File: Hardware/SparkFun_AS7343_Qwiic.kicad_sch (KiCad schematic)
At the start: 39 parts, among them J1 Qwiic_RA, J2 Qwiic_RA, J3 Conn_01x06, Q1 BSS138, Q2 BSS138, U1 RT9080-1.8V, U2 AS7343

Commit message: remove extra directory - resave in kicad 9.0
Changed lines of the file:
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@@
 (kicad_sch
-	(version 20231120)
+	(version 20250114)
 	(generator "eeschema")
-	(generator_version "8.0")
+	(generator_version "9.0")
 	(paper "USLetter")
 	(title_block
@@
 		(comment 2 "Designed by: P. Lewis")
 	)
+	(text "Low Pass\n7.2KHz"
+		(exclude_from_sim no)
+		(at 59.69 41.91 0)
+		(effects
+			(font
+				(size 1.27 1.27)
+				(color 132 132 132 1)
+			)
+		)
+	)
+	(text "D3 is DNP\nUsers may populate\ntheir own PTH LED \nas desired."
+		(exclude_from_sim no)
+		(at 142.24 53.34 0)
+		(effects
+			(font
+				(size 1.27 1.27)
+				(color 132 132 132 1)
+			)
+		)
+	)
+	(text "1.8V Voltage Regulator"
+		(exclude_from_sim no)
+		(at 113.03 91.44 0)
+		(effects
+			(font
+				(size 3 3)
+			)
+		)
+	)
+	(text "I²C Logic Level Conversion"
+		(exclude_from_sim no)
+		(at 210.82 20.32 0)
+		(effects
+			(font
+				(size 3 3)
+			)
+		)
+	)
+	(text "Cut jumper to turn off power LED"
+		(exclude_from_sim no)
+		(at 24.638 135.128 0)
+		(effects
+			(font
+				(size 1.27 1.27)
+				(color 132 132 132 1)
+			)
+			(justify left bottom)
+		)
+	)
+	(text "Cut jumper to disable \non-board White LED."
+		(exclude_from_sim no)
+		(at 129.54 76.2 0)
+		(effects
+			(font
+				(size 1.27 1.27)
+				(color 132 132 132 1)
+			)
+		)
+	)
+	(text "Power LED"
+		(exclude_from_sim no)
+		(at 40.64 91.44 0)
+		(effects
+			(font
+				(size 3 3)
+			)
+		)
+	)
+	(text "Connectors"
+		(exclude_from_sim no)
+		(at 78.74 151.13 0)
+		(effects
+			(font
+				(size 3 3)
+			)
+		)
+	)
+	(text "Spectral Sensor AS7343"
+		(exclude_from_sim no)
+		(at 77.47 20.32 0)
+		(effects
+			(font
+				(size 3 3)
+			)
+		)
+	)
 	(junction
 		(at 71.12 60.96)
@@
 		)
 	)
-	(text "Low Pass\n7.2KHz"
-		(exclude_from_sim no)
-		(at 59.69 41.91 0)
-		(effects
-			(font
-				(size 1.27 1.27)
-				(color 132 132 132 1)
-			)
-		)
-	)
-	(text "D3 is DNP\nUsers may populate\ntheir own PTH LED \nas desired."
-		(exclude_from_sim no)
-		(at 142.24 53.34 0)
-		(effects
-			(font
-				(size 1.27 1.27)
-				(color 132 132 132 1)
-			)
-		)
-	)
-	(text "1.8V Voltage Regulator"
-		(exclude_from_sim no)
-		(at 113.03 91.44 0)
-		(effects
-			(font
-				(size 3 3)
-			)
-		)
-	)
-	(text "I²C Logic Level Conversion"
-		(exclude_from_sim no)
-		(at 210.82 20.32 0)
-		(effects
-			(font
-				(size 3 3)
-			)
-		)
-	)
-	(text "Cut jumper to turn off power LED"
-		(exclude_from_sim no)
-		(at 24.638 135.128 0)
-		(effects
-			(font
-				(size 1.27 1.27)
-				(color 132 132 132 1)
-			)
-			(justify left bottom)
-		)
-	)
-	(text "Cut jumper to disable \non-board White LED."
-		(exclude_from_sim no)
-		(at 129.54 76.2 0)
-		(effects
-			(font
-				(size 1.27 1.27)
-				(color 132 132 132 1)
-			)
-		)
-	)
-	(text "Power LED"
-		(exclude_from_sim no)
-		(at 40.64 91.44 0)
-		(effects
-			(font
-				(size 3 3)
-			)
-		)
-	)
-	(text "Connectors"
-		(exclude_from_sim no)
-		(at 78.74 151.13 0)
-		(effects
-			(font
-				(size 3 3)
-			)
-		)
-	)
-	(text "Spectral Sensor AS7343"
-		(exclude_from_sim no)
-		(at 77.47 20.32 0)
-		(effects
-			(font
-				(size 3 3)
-			)
-		)
-	)
 	(global_label "SDA"
 		(shape input)
@@
 		(on_board yes)
 		(dnp no)
-		(property "Reference" "#PWR0124"
+		(property "Reference" "#PWR0107"
 			(at 125.73 193.04 0)
 			(effects
@@
 		(on_board yes)
 		(dnp no)
-		(property "Reference" "#PWR0124"
+		(property "Reference" "#PWR0123"
 			(at 34.29 190.5 0)
 			(effects
@@
 		(on_board yes)
 		(dnp no)
-		(property "Reference" "#PWR0124"
+		(property "Reference" "#PWR0105"
 			(at 76.2 190.5 0)
 			(effects
@@
 		)
 	)
+	(embedded_fonts no)
 )

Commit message: PROD_IDs
-prod IDs for IC and white LED
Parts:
- U2: PROD_ID (none) -> IC-26195
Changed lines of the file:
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@@
 			)
 		)
-		(property "Datasheet" ""
+		(property "Datasheet" "https://look.ams-osram.com/m/5f2d27fff9a874d2/original/AS7343-14-Channel-Multi-Spectral-Sensor.pdf"
 			(at 80.518 70.866 0)
 			(effects
@@
 			)
 		)
-		(property "PROD_ID" ""
+		(property "PROD_ID" "IC-26195"
 			(at 81.534 77.47 0)
 			(effects

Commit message: I2C address in sch and bottom silk
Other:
- note added: "I2C ADDRESS: 0x39"
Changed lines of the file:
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@@
+		)
+	)
+	(text "I2C ADDRESS: 0x39"
+		(exclude_from_sim no)
+		(at 82.55 72.39 0)
+		(effects
+			(font
+				(size 1.27 1.27)
+				(color 132 132 132 1)
+			)
 		)
 	)

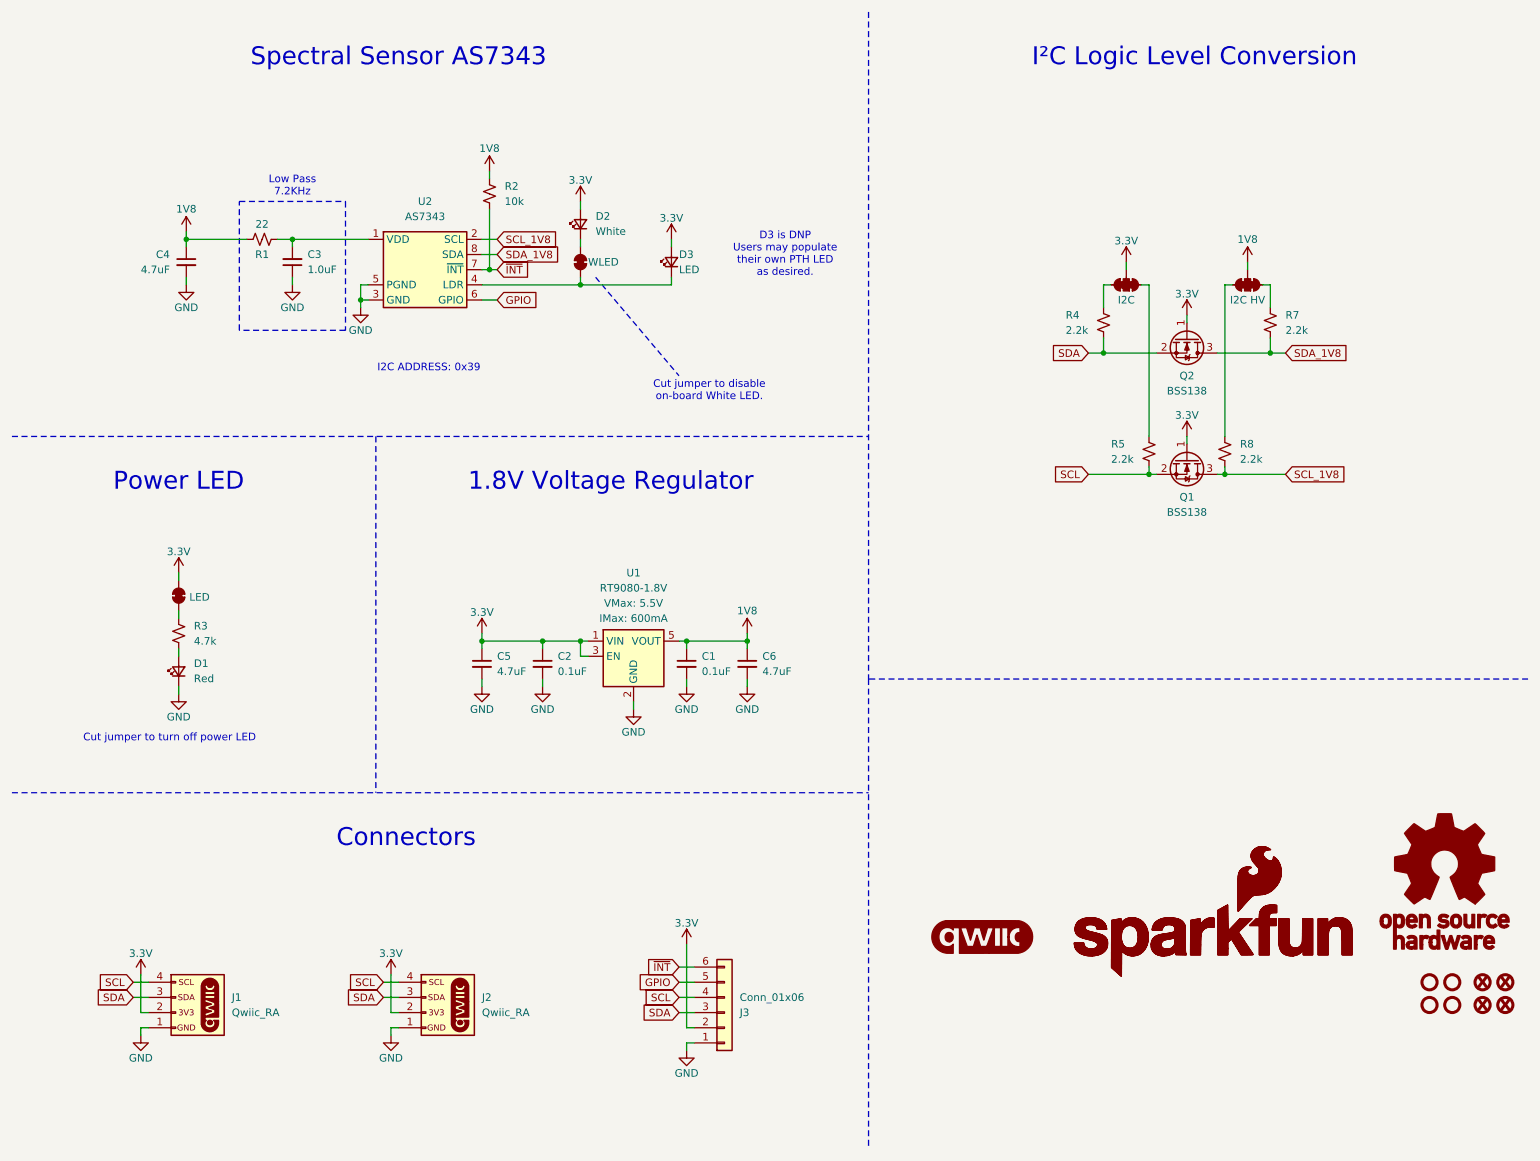
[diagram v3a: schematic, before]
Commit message: checklist run eng
-sch tightening
-vcc range added to sch
-removed PROD_ID from DNP LED
-add 1.8V testpoint
-increased copper to dimension clearance from 3 mils to 8 mils (avoiding sanding damage)
-nudged qwiic connectors inward from the edge by 5mils (avoiding sanding damage)
-updated pin one marker on IC from triangle to dot
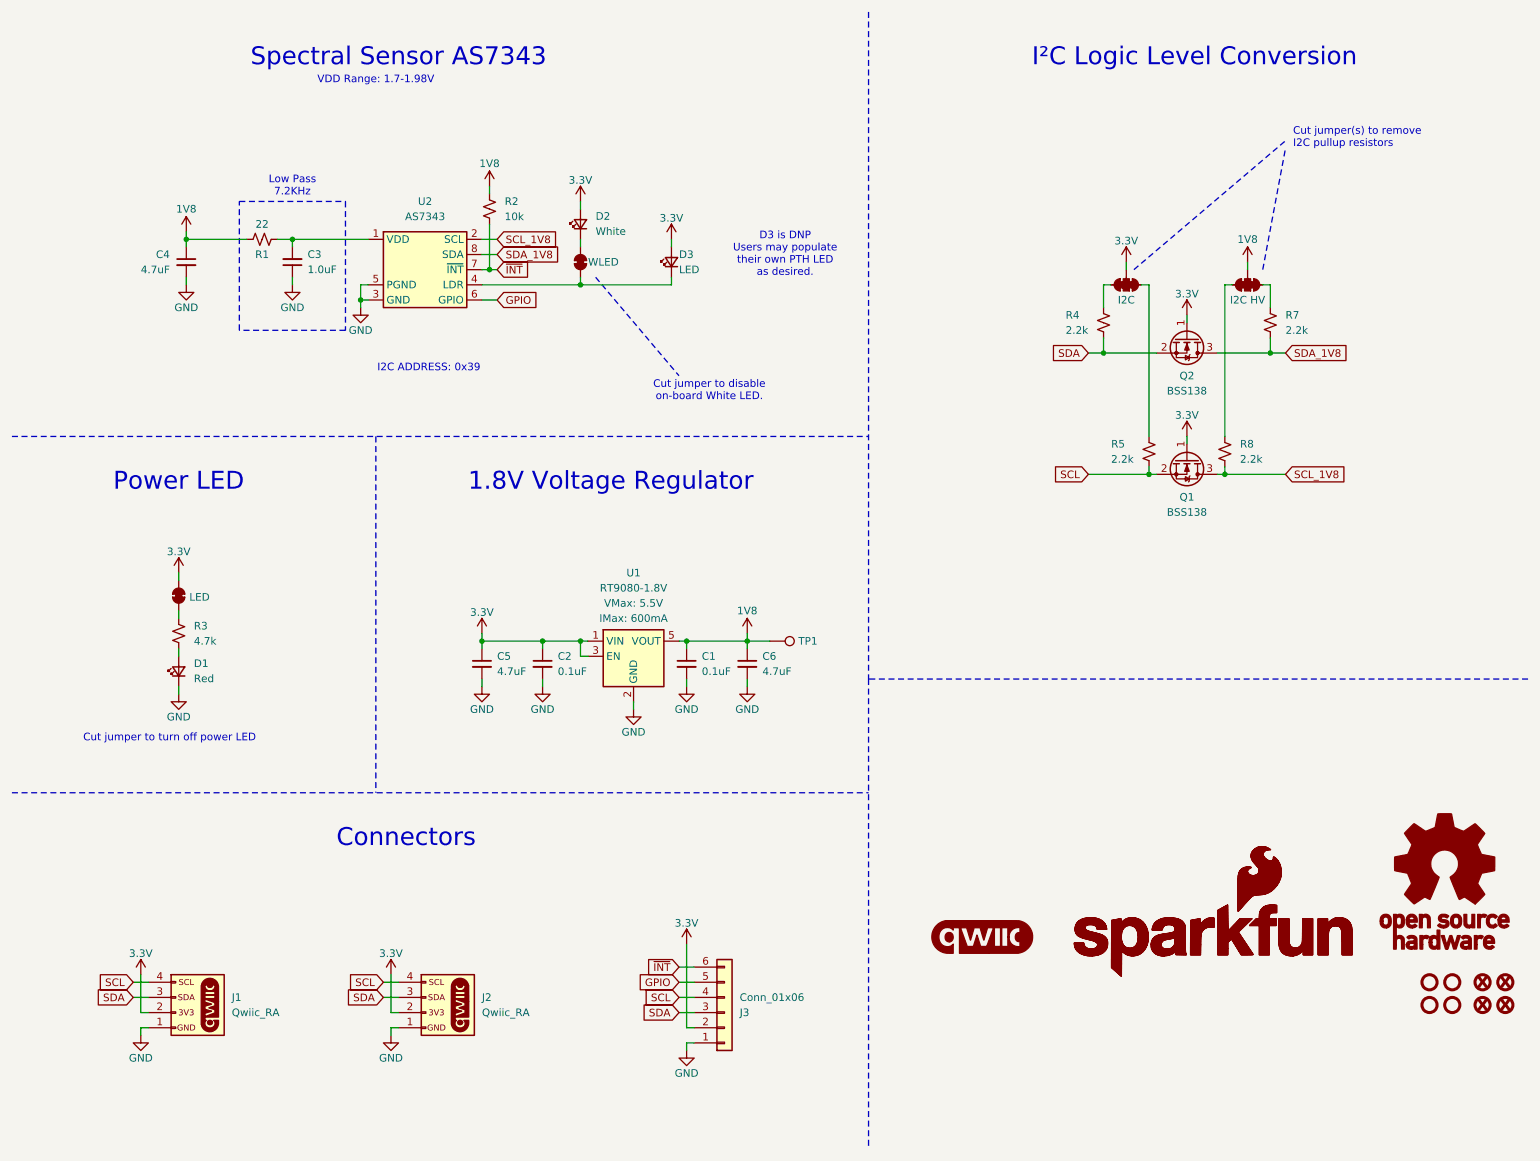
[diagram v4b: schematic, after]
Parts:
- added TP1: 1.0mm, SparkFun-Connector:TestPoint-1.0mm, symbol SparkFun-Connector:TestPoint_1.0mm
- D3: PROD_ID LED- -> (none)
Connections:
- net 1V8: now also TP1.1
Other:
- note added: "Cut jumper(s) to remove I2C pullup resistors"
- note added: "VDD Range: 1.7-1.98V"
- moved on the sheet: R2
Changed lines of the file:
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@@
 		)
 	)
+	(text "Cut jumper(s) to remove \nI2C pullup resistors"
+		(exclude_from_sim no)
+		(at 227.33 35.56 0)
+		(effects
+			(font
+				(size 1.27 1.27)
+				(color 132 132 132 1)
+			)
+			(justify left bottom)
+		)
+	)
 	(text "1.8V Voltage Regulator"
 		(exclude_from_sim no)
@@
 		)
 	)
+	(text "VDD Range: 1.7-1.98V"
+		(exclude_from_sim no)
+		(at 73.66 24.13 0)
+		(effects
+			(font
+				(size 1.27 1.27)
+				(color 132 132 132 1)
+			)
+		)
+	)
 	(text "Connectors"
 		(exclude_from_sim no)
@@
 	(wire
 		(pts
-			(xy 92.71 39.37) (xy 92.71 40.64)
+			(xy 92.71 41.91) (xy 92.71 43.18)
 		)
 		(stroke
@@
 	(wire
 		(pts
-			(xy 92.71 45.72) (xy 92.71 55.88)
+			(xy 92.71 48.26) (xy 92.71 55.88)
 		)
 		(stroke
@@
 		)
 	)
+	(polyline
+		(pts
+			(xy 200.66 55.88) (xy 226.06 34.29)
+		)
+		(stroke
+			(width 0)
+			(type dash)
+			(color 132 132 132 1)
+		)
+	)
 	(wire
 		(pts
@@
 	(wire
 		(pts
+			(xy 135.89 118.11) (xy 139.7 118.11)
+		)
+		(stroke
+			(width 0)
+			(type default)
+		)
+	)
+	(wire
+		(pts
 			(xy 91.44 118.11) (xy 101.6 118.11)
 		)
@@
 	(polyline
 		(pts
+			(xy 222.25 55.88) (xy 226.06 35.56)
+		)
+		(stroke
+			(width 0)
+			(type dash)
+			(color 132 132 132 1)
+		)
+	)
+	(polyline
+		(pts
 			(xy 50.8 66.04) (xy 50.8 44.45)
 		)
@@
 	)
 	(symbol
+		(lib_id "SparkFun-Connector:TestPoint_1.0mm")
+		(at 139.7 118.11 270)
+		(unit 1)
+		(exclude_from_sim no)
+		(in_bom yes)
+		(on_board yes)
+		(dnp no)
+		(property "Reference" "TP1"
+			(at 146.05 118.11 90)
+			(do_not_autoplace yes)
+			(effects
+				(font
+					(size 1.27 1.27)
+				)
+			)
+		)
+		(property "Value" "1.0mm"
+			(at 135.89 118.11 0)
+			(effects
+				(font
+					(size 1.27 1.27)
+				)
+				(hide yes)
+			)
+		)
+		(property "Footprint" "SparkFun-Connector:TestPoint-1.0mm"
+			(at 133.35 118.11 0)
+			(effects
+				(font
+					(size 1.27 1.27)
+				)
+				(hide yes)
+			)
+		)
+		(property "Datasheet" "~"
+			(at 132.08 118.11 0)
+			(effects
+				(font
+					(size 1.27 1.27)
+				)
+				(hide yes)
+			)
+		)
+		(property "Description" "Test Point"
+			(at 129.54 118.11 0)
+			(effects
+				(font
+					(size 1.27 1.27)
+				)
+				(hide yes)
+			)
+		)
+		(pin "1"
+		)
+		(instances
+			(project ""
+				(path "/e3dd3ae4-244d-4cba-9cca-5d2abf83f29a"
+					(reference "TP1")
+					(unit 1)
+				)
+			)
+		)
+	)
+	(symbol
 		(lib_id "SparkFun-Resistor:2.2k_0603")
 		(at 195.58 64.77 90)
@@
 	(symbol
 		(lib_id "SparkFun-Resistor:10k_0603")
-		(at 92.71 43.18 90)
+		(at 92.71 45.72 90)
 		(unit 1)
 		(exclude_from_sim no)
@@
 		(fields_autoplaced yes)
 		(property "Reference" "R2"
-			(at 95.25 41.9099 90)
+			(at 95.25 44.4499 90)
 			(effects
 				(font
@@
 		)
 		(property "Value" "10k"
-			(at 95.25 44.4499 90)
+			(at 95.25 46.9899 90)
 			(effects
 				(font
@@
 		)
 		(property "Footprint" "SparkFun-Resistor:R_0603_1608Metric"
-			(at 97.028 43.18 0)
+			(at 97.028 45.72 0)
 			(effects
 				(font
@@
 		)
 		(property "Datasheet" "https://www.vishay.com/docs/20035/dcrcwe3.pdf"
-			(at 101.6 43.18 0)
+			(at 101.6 45.72 0)
 			(effects
 				(font
@@
 		)
 		(property "Description" "Resistor"
-			(at 104.14 43.18 0)
+			(at 104.14 45.72 0)
 			(effects
 				(font
@@
 		)
 		(property "PROD_ID" "RES-00824"
-			(at 99.06 43.18 0)
+			(at 99.06 45.72 0)
 			(effects
 				(font
@@
 			)
 		)
-		(property "PROD_ID" "LED-"
-			(at 133.35 54.61 0)
-			(effects
-				(font
-					(size 1.27 1.27)
-				)
-				(hide yes)
-			)
-		)
 		(pin "2"
 		)
@@
 	(symbol
 		(lib_id "SparkFun-PowerSymbol:VCC")
-		(at 92.71 39.37 0)
+		(at 92.71 41.91 0)
 		(unit 1)
 		(exclude_from_sim no)
@@
 		(fields_autoplaced yes)
 		(property "Reference" "#PWR09"
-			(at 92.71 43.18 0)
+			(at 92.71 45.72 0)
 			(effects
 				(font
@@
 		)
 		(property "Value" "1V8"
-			(at 92.71 35.56 0)
+			(at 92.71 38.1 0)
 			(do_not_autoplace yes)
 			(effects
@@
 		)
 		(property "Footprint" ""
-			(at 92.71 39.37 0)
+			(at 92.71 41.91 0)
 			(effects
 				(font
@@
 		)
 		(property "Datasheet" ""
-			(at 92.71 39.37 0)
+			(at 92.71 41.91 0)
 			(effects
 				(font
@@
 		)
 		(property "Description" "Power symbol creates a global label with name \"VCC\""
-			(at 92.71 45.72 0)
+			(at 92.71 48.26 0)
 			(effects
 				(font

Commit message: more review catches
-Checked the properties box for DNP on D3, also exclude from BOM.
-sch cleanup
-removed isolation jumper for 1v8 i2c pullups
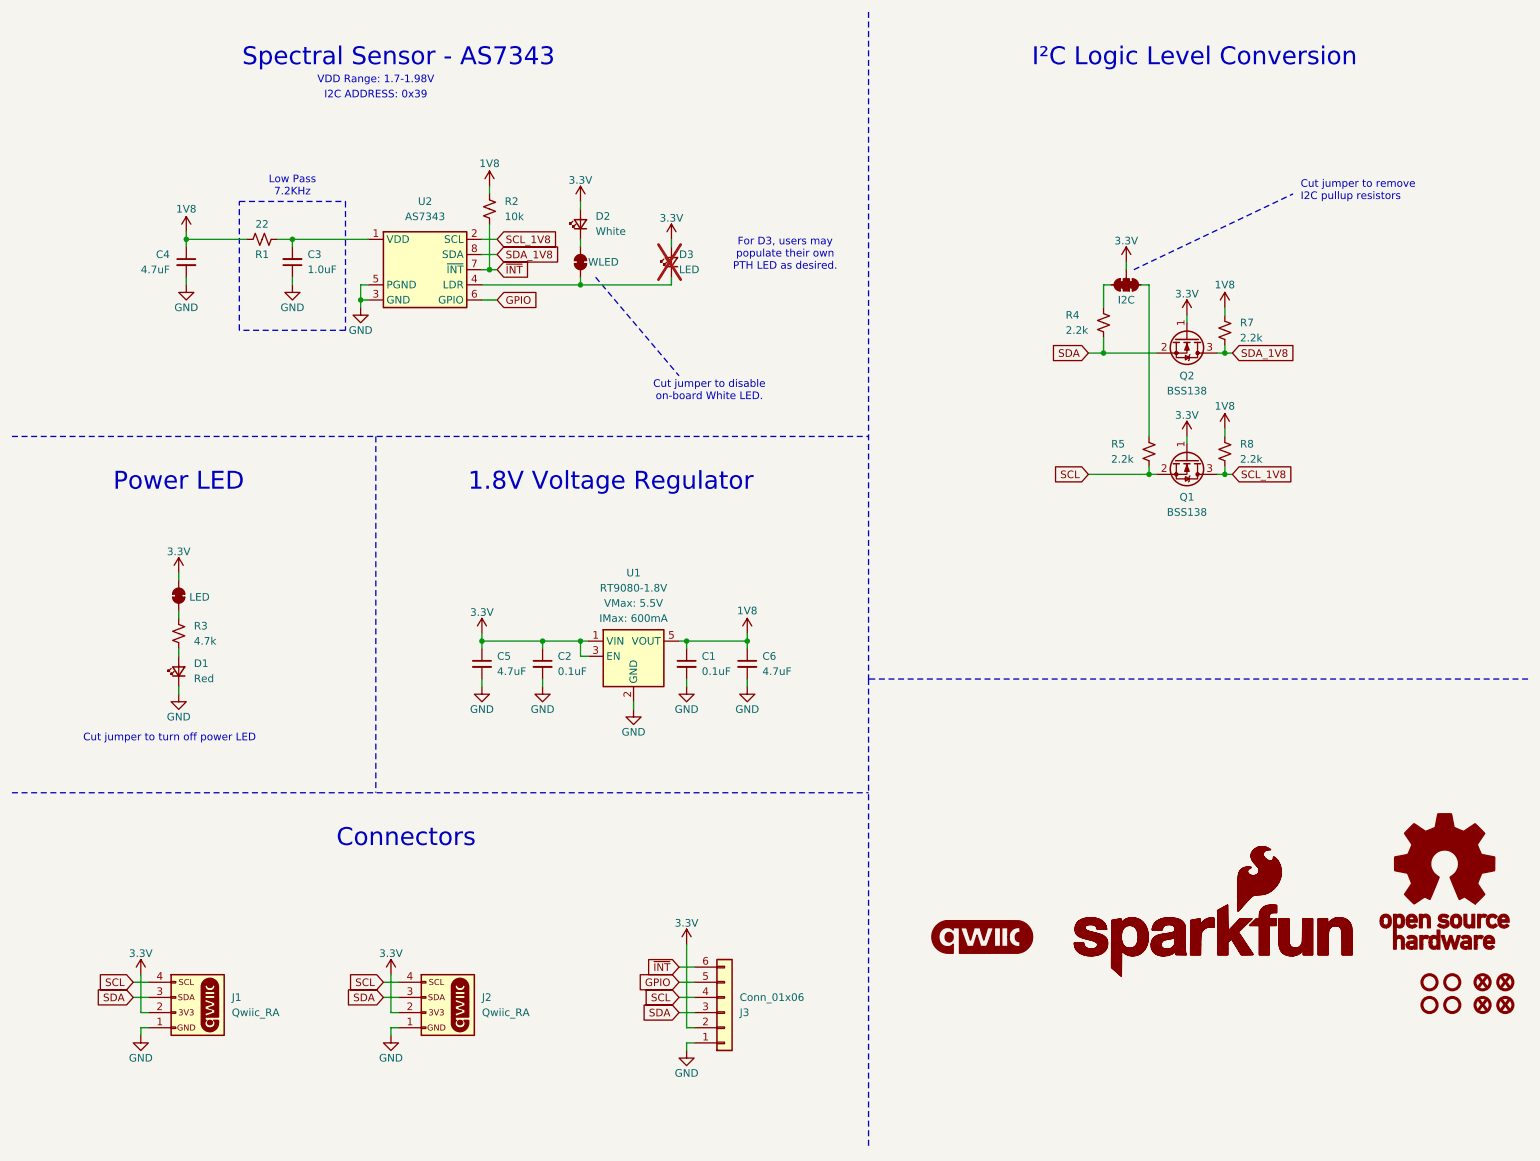
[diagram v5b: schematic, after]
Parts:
- removed JP4: I2C HV, SparkFun-Jumper:Jumper_3_NC-2_Trace, symbol SparkFun-Jumper:SolderJumper_3_Bridged123
- removed TP1: 1.0mm, SparkFun-Connector:TestPoint-1.0mm, symbol SparkFun-Connector:TestPoint_1.0mm
- D3: now not fitted; now left out of the parts list
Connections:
- net 1V8: now also R7.1, R8.1
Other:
- note added: "Cut jumper to remove I2C pullup resistors"
- note added: "For D3, users may populate their own PTH LED as desired."
- note added: "Spectral Sensor - AS7343"
- note removed: "Cut jumper(s) to remove I2C pullup resistors"
- note removed: "D3 is DNP Users may populate their own PTH LED as desired."
- note removed: "Spectral Sensor AS7343"
- moved on the sheet: R7
